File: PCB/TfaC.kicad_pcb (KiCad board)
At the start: 2 copper layers, 105 x 54 mm, 51 parts, among them IC501 ATMEGA88-A, M301 DisplayModule, P101 Line, P501 PRG, Q401 IRLML2502, Q402 IRLML2502, Q403 IRLML2502, Q404 IRLML2502, Q405 IRLML2502, Q406 IRLML2502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

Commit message: 2L.2 board corrections
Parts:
- added REF**: MountingHole_4mm, Mounting_Holes:MountingHole_4mm, F.Cu at (149.5, 74.0)
- moved SW508 2.52 mm to (159.0, 73.8)
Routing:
- net Alarm_Enabled: track 22.5 -> 24.5 mm
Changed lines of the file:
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@@
   (general
     (links 140)
-    (no_connects 0)
-    (area 94.440438 64.0139 211.811986 121.665724)
+    (no_connects 1)
+    (area 96.399999 64.899999 201.600001 119.100001)
     (thickness 1.6)
     (drawings 65)
-    (tracks 480)
+    (tracks 481)
     (zones 0)
-    (modules 51)
+    (modules 52)
     (nets 44)
   )
   (page A4)
   (layers
-    (0 F.Cu signal hide)
-    (31 B.Cu signal hide)
+    (0 F.Cu signal)
+    (31 B.Cu signal)
     (32 B.Adhes user)
     (33 F.Adhes user)
@@
     (pad_to_paste_clearance 0.0254)
     (aux_axis_origin 0 0)
-    (visible_elements 7FFEEF7F)
+    (visible_elements 7FFEFF7F)
     (pcbplotparams
       (layerselection 0x010fc_80000001)
@@
   )
   (module tfac-footprints:CLSB12C01 (layer F.Cu)
-    (at 161.5186 73.9902)
+    (at 159.004 73.787)
     (fp_text reference SW508 (at 2.4892 3.7338 180) (layer F.SilkS)
       (effects (font (size 0.762 0.762) (thickness 0.127)))
@@
       (xy 1.195199 0.12652) (xy 1.195199 0.12652)) (layer F.SilkS) (width 0.1))
   )
+  (module Mounting_Holes:MountingHole_4mm (layer F.Cu)
+    (at 149.479 74.041)
+    (descr "Mounting hole, Befestigungsbohrung, 4mm, No Annular, Kein Restring,")
+    (tags "Mounting hole, Befestigungsbohrung, 4mm, No Annular, Kein Restring,")
+    (fp_text reference REF** (at 0 -5.4991) (layer F.SilkS)
+      (effects (font (size 1 1) (thickness 0.15)))
+    )
+    (fp_text value MountingHole_4mm (at 0 5.99948) (layer F.Fab)
+      (effects (font (size 1 1) (thickness 0.15)))
+    )
+    (fp_circle (center 0 0) (end 4 0) (layer Cmts.User) (width 0.381))
+    (pad 1 thru_hole circle (at 0 0) (size 4 4) (drill 4) (layers))
+  )
   (gr_line (start 141.5 72) (end 141.5 65) (angle 90) (layer Edge.Cuts) (width 0.2))
   (gr_line (start 141.5 65) (end 201.5 65) (angle 90) (layer Edge.Cuts) (width 0.2))
@@
     (effects (font (size 0.762 0.762) (thickness 0.127)))
   )
-  (gr_text "Alarm Enable" (at 162.1536 78.7654) (layer F.SilkS)
+  (gr_text "Alarm Enable" (at 159.385 78.613) (layer F.SilkS)
     (effects (font (size 0.762 0.762) (thickness 0.127)))
   )
@@
   (segment (start 120.014086 79.877803) (end 121.827327 79.877803) (width 0.6096) (layer F.Cu) (net 4))
   (segment (start 121.827327 79.877803) (end 122.383326 80.433802) (width 0.6096) (layer F.Cu) (net 4))
-  (segment (start 165.9382 84.068) (end 165.1448 84.068) (width 0.3048) (layer F.Cu) (net 5))
-  (segment (start 161.5186 80.4418) (end 161.5186 72.3402) (width 0.3048) (layer F.Cu) (net 5))
-  (segment (start 165.1448 84.068) (end 161.5186 80.4418) (width 0.3048) (layer F.Cu) (net 5))
-  (segment (start 165.856 84.068) (end 165.9382 84.068) (width 0.3048) (layer F.Cu) (net 5))
+  (segment (start 165.862 84.068) (end 163.697 84.068) (width 0.3048) (layer F.Cu) (net 5))
+  (segment (start 159.004 79.375) (end 159.004 72.137) (width 0.3048) (layer F.Cu) (net 5))
+  (segment (start 163.697 84.068) (end 159.004 79.375) (width 0.3048) (layer F.Cu) (net 5))
+  (segment (start 165.856 84.068) (end 165.862 84.068) (width 0.3048) (layer F.Cu) (net 5))
+  (segment (start 165.862 84.068) (end 165.9382 84.068) (width 0.3048) (layer F.Cu) (net 5))
   (segment (start 165.9382 84.068) (end 174.312 84.068) (width 0.3048) (layer F.Cu) (net 5))
   (segment (start 188.125 82.075) (end 188.475 82.075) (width 0.6096) (layer B.Cu) (net 6))

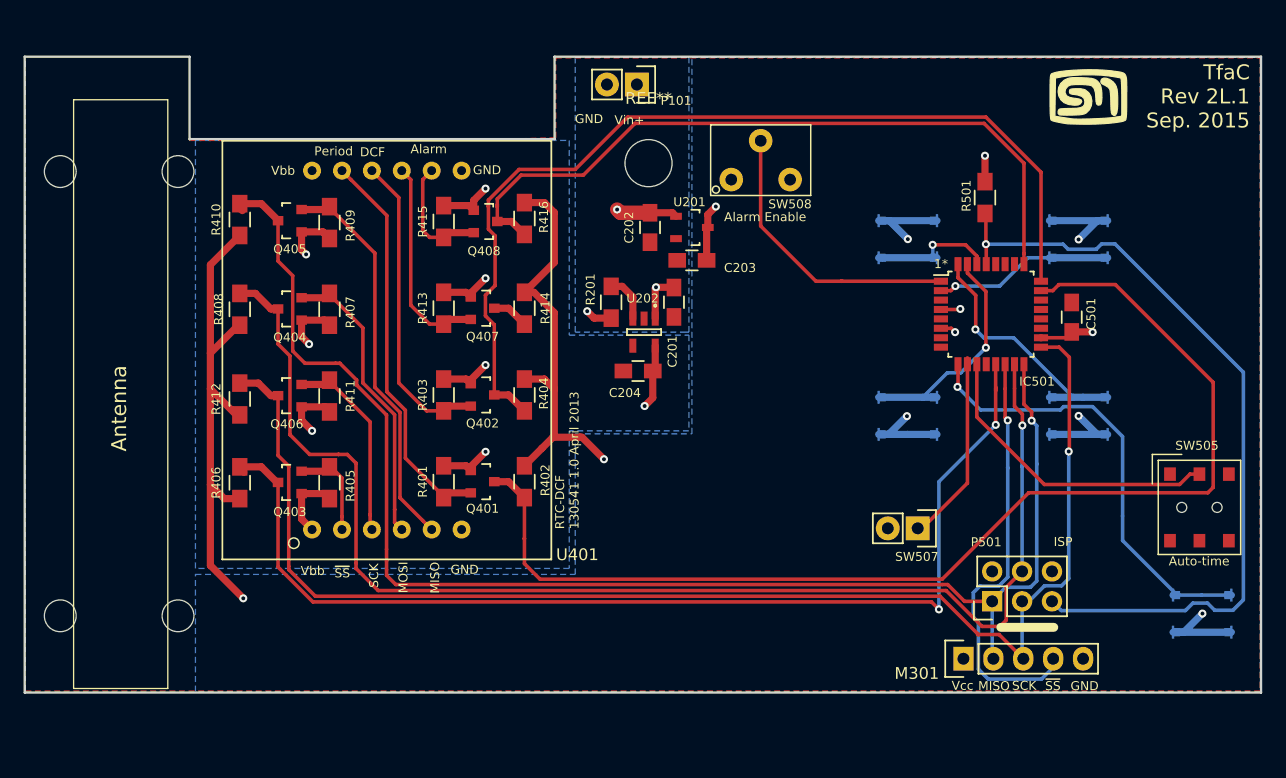
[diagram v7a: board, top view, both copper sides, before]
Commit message: Made corrections to the board for rev 2L.2
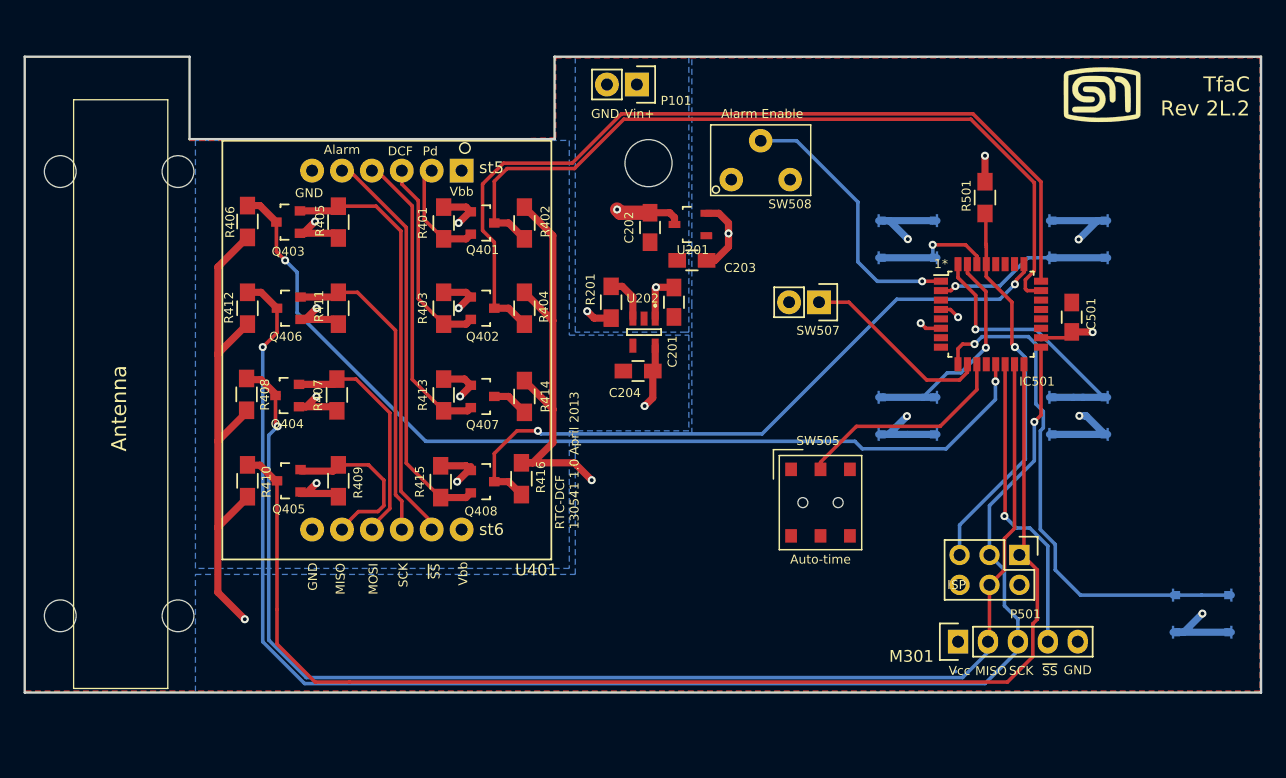
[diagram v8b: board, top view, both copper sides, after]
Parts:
- removed the G*** at (186.8, 68.4)
- added G***: LOGO, tfac-footprints:sm-logo-1200, F.Cu at (188.1, 68.1)
- moved SW505 32.2 mm to (164.1, 102.9)
- moved R406 22.2 mm to (115.4, 79.0)
- moved R410 22.2 mm to (115.4, 101.0)
- moved R405 22.1 mm to (123.1, 79.0)
- moved Q403 22.1 mm to (118.9, 79.0)
- moved Q408 22.1 mm to (135.4, 101.1)
- moved R415 22.1 mm to (131.8, 101.1)
- moved R416 22.1 mm to (138.7, 100.8)
- moved Q405 22.1 mm to (118.9, 101.0)
- moved Q401 22.0 mm to (135.4, 79.1)
- moved R401 22.0 mm to (132.1, 79.1)
- moved R402 22.0 mm to (138.9, 79.1)
- moved R409 21.9 mm to (123.1, 101.0)
- moved SW507 21.0 mm to (164.0, 85.9)
- moved R412 7.74 mm to (115.4, 86.4)
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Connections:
- M301 pad 2: /Controller/MISO -> /Controller/MOSI
- U201 pad 1: /Power System/Vin -> GND
- U201 pad 2: GND -> /Controller/Vcc
- U201 pad 3: /Controller/Vcc -> /Power System/Vin
- U401 pad 10: L_Rx -> L_MOSI
- U401 pad 11: L_ALARM_INT -> L_MISO
- U401 pad 2: ~L_SS -> L_Periodic_INT
- U401 pad 3: L_SCK -> L_DCF_RCPT
- U401 pad 4: L_MOSI -> L_Rx
- U401 pad 5: L_MISO -> L_ALARM_INT
- U401 pad 8: L_Periodic_INT -> ~L_SS
- U401 pad 9: L_DCF_RCPT -> L_SCK
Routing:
- net Reset: track 68.1 -> 33.9 mm
- net /Controller/Periodic_INT: track 98.2 -> 67.7 mm
- net ~L_SS: track 8.47 -> 36.0 mm
- net L_Periodic_INT: track 33.8 -> 9.28 mm
- net L_ALARM_INT: track 10.1 -> 34.4 mm
- net L_MISO: track 33.5 -> 14.4 mm
- net /Controller/~RTC_SELECT: track 92.5 -> 80.3 mm
- net /Controller/SCK: track 116.3 -> 128.4 mm, vias 1 -> 2
- net /Controller/MISO: track 120.9 -> 109.7 mm, vias 1 -> 0
- net /Controller/~DISPLAY_SELECT: track 36.8 -> 26.1 mm
- net L_SCK: track 16.7 -> 26.7 mm
- net L_DCF_RCPT: track 26.2 -> 17.0 mm
- net L_Rx: track 17.7 -> 25.6 mm
- net Auto_Time: track 26.1 -> 18.6 mm
- net /Controller/DCF_RCPT: track 81.7 -> 74.8 mm
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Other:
- board text added: "Pd"
- board text added: "TfaC Rev 2L.2"
- board text removed: "Period"
- board text removed: "TfaC Rev 2L.1 Sep. 2015"
